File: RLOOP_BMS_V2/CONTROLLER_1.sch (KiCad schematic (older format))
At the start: 29 parts, among them U3 bq76PL536A_HTQFP

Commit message: More WIP
Added connector for 1-Wire sensors if we want to put some sensors on the
heat-sinks. Just need to double check everything with the 3d-models.
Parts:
- U3: symbol bq76PL536A_HTQFP -> bq76PL536A_HTQFP-RESCUE-rLoop_BMS_v2
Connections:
- net labels added: ALERT_H, CONV_H, DRDY_H, FAULT_H
- wire segments 133 -> 138
- no-connect marks 5 -> 1
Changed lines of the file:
@@
 EESchema Schematic File Version 2
+LIBS:rLoop BMS v2-rescue
 LIBS:power
 LIBS:device
@@
 Text GLabel 4700 5750 3    60   Input ~ 0
 GND_1
-NoConn ~ 5200 5100
-NoConn ~ 5300 5100
-NoConn ~ 5400 5100
-NoConn ~ 5500 5100
-$Comp
-L bq76PL536A_HTQFP U3
+$Comp
+L bq76PL536A_HTQFP-RESCUE-rLoop_BMS_v2 U3
 U 1 1 592C9A06
 P 5550 3650
+AR Path="/592C9A06" Ref="U3"  Part="1"
+AR Path="/590D88AD/592C9A06" Ref="U3"  Part="1"
 F 0 "U3" H 5550 3650 60  0000 C CNN
 F 1 "bq76PL536A_HTQFP" H 5550 3900 60  0000 C CNN
@@
 	4300 3750 4400 3750
 Wire Wire Line
-	4300 3550 4300 3750
+	4300 3450 4300 3750
 Wire Wire Line
 	4250 3550 4400 3550
@@
 Wire Wire Line
 	8800 1500 8800 1450
+Text HLabel 5200 5750 3    60   Output ~ 0
+FAULT_H
+Text HLabel 5300 5750 3    60   Output ~ 0
+ALERT_H
+Text HLabel 5400 5750 3    60   Output ~ 0
+DRDY_H
+Text HLabel 5500 5750 3    60   Input ~ 0
+CONV_H
+Wire Wire Line
+	5500 5750 5500 5100
+Wire Wire Line
+	5400 5100 5400 5750
+Wire Wire Line
+	5300 5750 5300 5100
+Wire Wire Line
+	5200 5100 5200 5750
+Wire Wire Line
+	4400 3450 4300 3450
 $EndSCHEMATC

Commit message: more WIP
So close. Need to finish arranging the sild screen and make sure diodes
get put on in the correct orientation.
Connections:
- net GND_1: now also U3.THRM
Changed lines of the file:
@@
 Connection ~ 7500 3800
 Wire Wire Line
-	7100 4250 7100 4900
+	7100 4150 7100 4900
 Wire Wire Line
 	6650 4250 7100 4250
@@
 Wire Wire Line
 	4400 3450 4300 3450
+Wire Wire Line
+	6650 4150 7100 4150
+Connection ~ 7100 4250
 $EndSCHEMATC

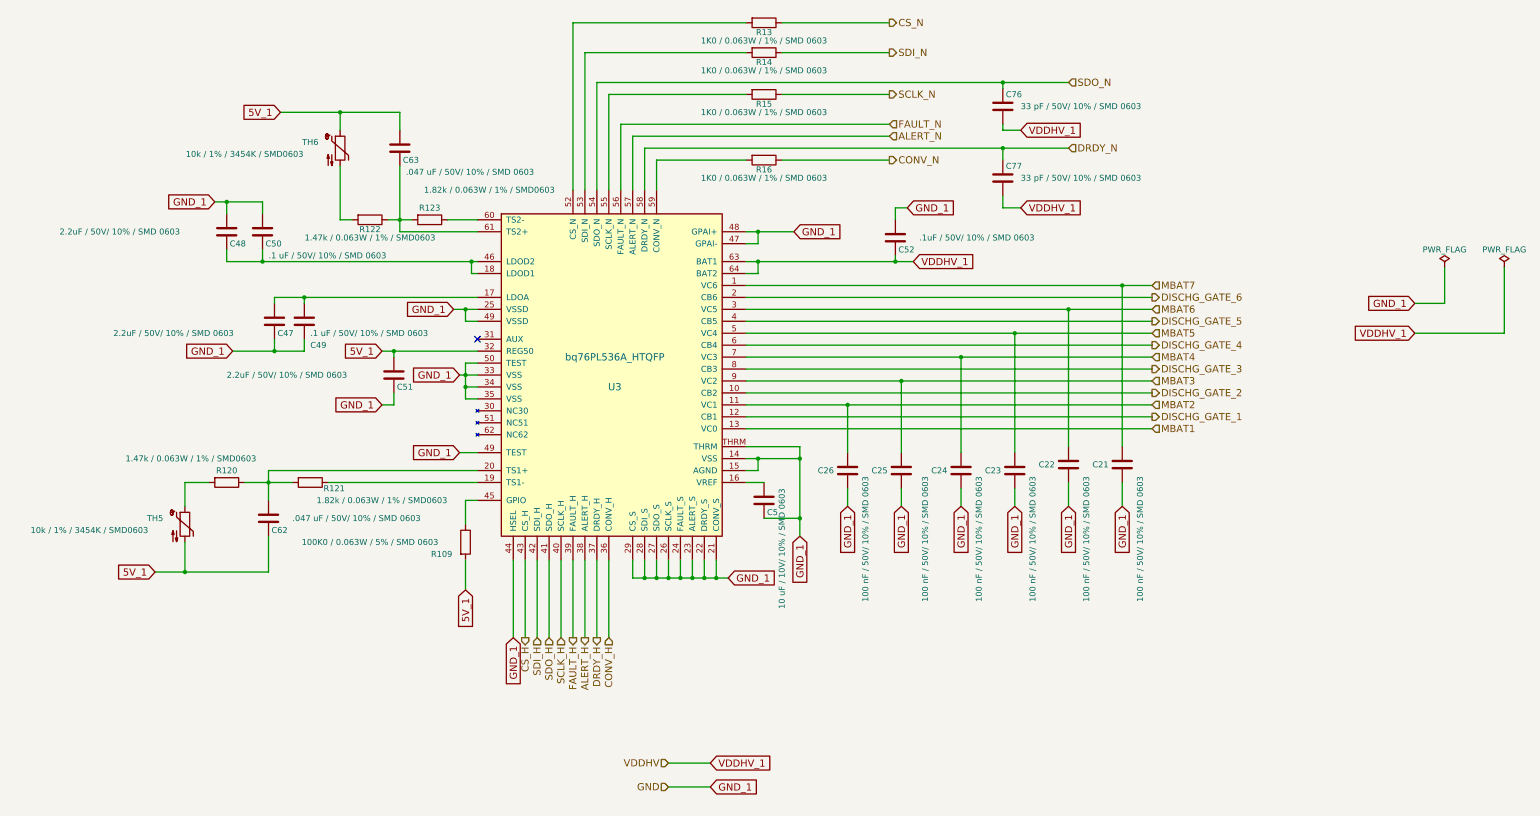
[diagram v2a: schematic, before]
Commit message: Updated page sizes for schematics
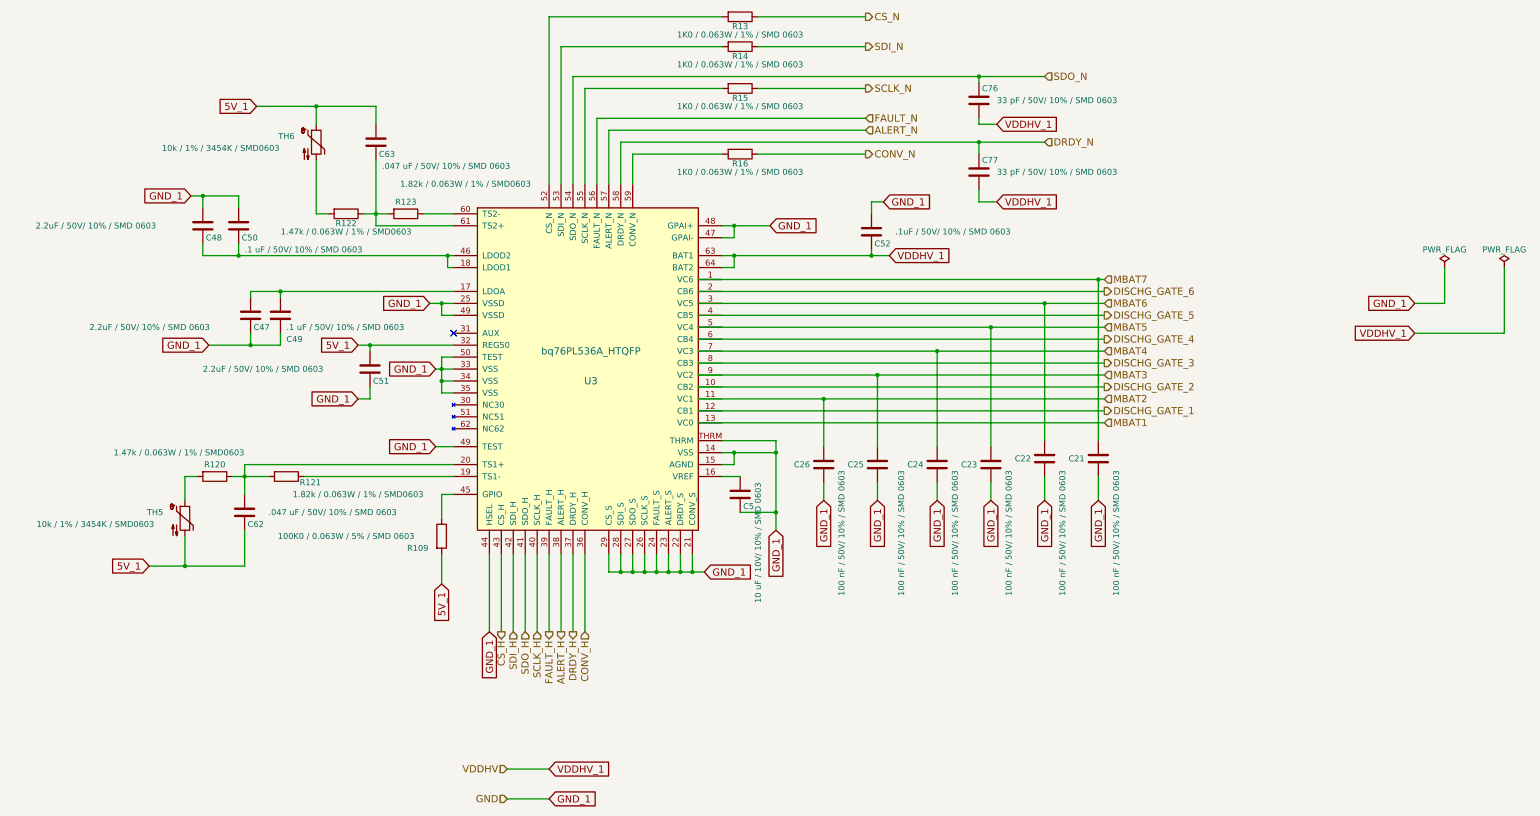
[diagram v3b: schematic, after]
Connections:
- wire segments 139 -> 176
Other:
- moved on the sheet: C21, C22, C23, C24, C25, C26, C47, C48, C49, C5, C50, C51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

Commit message: swapped a few connectors to standardize with the power node and what's readily available
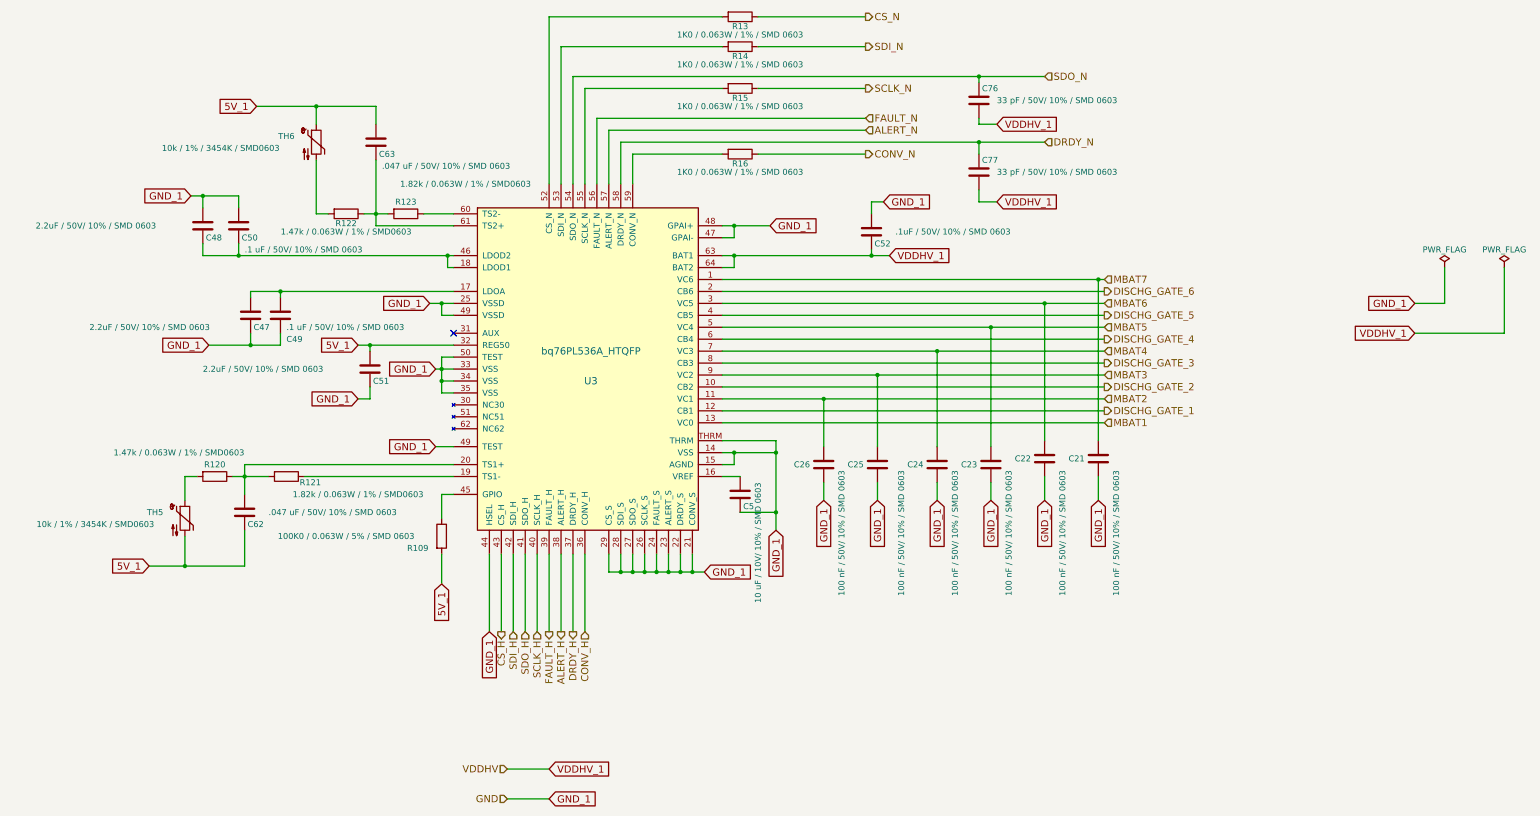
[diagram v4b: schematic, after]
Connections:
- wire segments 176 -> 139
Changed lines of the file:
@@
 	4650 7100 5000 7100
 Wire Wire Line
-	6250 2750 9600 2750
-Wire Wire Line
-	9600 2750 9650 2750
-Wire Wire Line
-	9650 2850 6250 2850
-Wire Wire Line
-	6250 3050 9650 3050
-Wire Wire Line
-	6250 2950 9150 2950
-Wire Wire Line
-	9150 2950 9650 2950
-Wire Wire Line
-	6250 3150 8700 3150
-Wire Wire Line
-	8700 3150 9650 3150
-Wire Wire Line
-	9650 3250 6250 3250
-Wire Wire Line
-	6250 3350 8250 3350
-Wire Wire Line
-	8250 3350 9650 3350
-Wire Wire Line
-	9650 3450 6250 3450
-Wire Wire Line
-	6450 2550 6550 2550
-Wire Wire Line
-	6550 2550 7700 2550
-Wire Wire Line
-	7700 2550 7850 2550
+	6450 2750 9650 2750
+Wire Wire Line
+	6450 2950 9650 2950
+Wire Wire Line
+	6450 3150 9650 3150
+Wire Wire Line
+	6450 3350 9650 3350
+Wire Wire Line
+	6450 2550 7850 2550
 Wire Wire Line
 	6450 2650 6550 2650
@@
 Connection ~ 6550 2550
 Wire Wire Line
-	6250 3550 7750 3550
-Wire Wire Line
-	7750 3550 9650 3550
-Wire Wire Line
-	9650 3650 6250 3650
-Wire Wire Line
-	6250 3750 7300 3750
-Wire Wire Line
-	7300 3750 9650 3750
-Wire Wire Line
-	9650 3850 6250 3850
-Wire Wire Line
-	6250 3950 9650 3950
+	6450 3550 9650 3550
+Wire Wire Line
+	6450 3750 9650 3750
 Wire Wire Line
 	9600 4600 9600 4400
@@
 Connection ~ 7300 3750
 Wire Wire Line
-	6900 4100 6900 4200
-Wire Wire Line
-	6900 4200 6900 4700
-Wire Wire Line
-	6900 4700 6900 4850
-Wire Wire Line
-	6450 4200 6550 4200
-Wire Wire Line
-	6550 4200 6900 4200
+	6900 4100 6900 4850
+Wire Wire Line
+	6450 4200 6900 4200
 Wire Wire Line
 	6450 4300 6550 4300
@@
 	4100 3700 4200 3700
 Wire Wire Line
-	4100 3400 4100 3500
-Wire Wire Line
-	4100 3500 4100 3600
-Wire Wire Line
-	4100 3600 4100 3700
-Wire Wire Line
-	4050 3500 4100 3500
-Wire Wire Line
-	4100 3500 4200 3500
+	4100 3400 4100 3700
+Wire Wire Line
+	4050 3500 4200 3500
 Connection ~ 4100 3500
 Wire Wire Line
@@
 Connection ~ 4100 3600
 Wire Wire Line
-	4000 2950 4100 2950
-Wire Wire Line
-	4100 2950 4200 2950
+	4000 2950 4200 2950
 Wire Wire Line
 	4200 3050 4100 3050
@@
 Connection ~ 4100 2950
 Wire Wire Line
-	3400 3300 3500 3300
-Wire Wire Line
-	3500 3300 4200 3300
+	3400 3300 4200 3300
 Wire Wire Line
 	4050 4150 4200 4150
 Wire Wire Line
-	5500 5200 5600 5200
-Wire Wire Line
-	5600 5200 5700 5200
-Wire Wire Line
-	5700 5200 5800 5200
-Wire Wire Line
-	5800 5200 5900 5200
-Wire Wire Line
-	5900 5200 6000 5200
-Wire Wire Line
-	6000 5200 6100 5200
-Wire Wire Line
-	6100 5200 6200 5200
-Wire Wire Line
-	6200 5200 6300 5200
+	5500 5200 6300 5200
 Wire Wire Line
 	6200 5200 6200 5050
@@
 Connection ~ 5600 5200
 Wire Wire Line
-	6450 2300 6550 2300
-Wire Wire Line
-	6550 2300 6850 2300
+	6450 2300 6850 2300
 Wire Wire Line
 	6450 2400 6550 2400
@@
 	5600 1950 5600 1600
 Wire Wire Line
-	5600 1600 8600 1600
-Wire Wire Line
-	8600 1600 9150 1600
+	5600 1600 9150 1600
 Wire Wire Line
 	5700 1950 5700 1700
@@
 	3500 3750 3500 3650
 Wire Wire Line
-	2000 2050 2100 2050
-Wire Wire Line
-	2100 2050 2400 2050
+	2000 2050 2400 2050
 Wire Wire Line
 	2100 2050 2100 2150
@@
 	2100 2450 2100 2550
 Wire Wire Line
-	2100 2550 2400 2550
-Wire Wire Line
-	2400 2550 4150 2550
-Wire Wire Line
-	4150 2550 4200 2550
+	2100 2550 4200 2550
 Wire Wire Line
 	2400 2450 2400 2550
@@
 	2500 2900 2500 2850
 Wire Wire Line
-	2500 2850 2750 2850
-Wire Wire Line
-	2750 2850 4200 2850
+	2500 2850 4200 2850
 Wire Wire Line
 	2750 2850 2750 2900
@@
 Connection ~ 4150 2550
 Wire Wire Line
-	2150 3300 2500 3300
-Wire Wire Line
-	2500 3300 2750 3300
+	2150 3300 2750 3300
 Wire Wire Line
 	2500 3300 2500 3200
@@
 	3550 2300 4200 2300
 Wire Wire Line
-	3550 1750 3550 2200
-Wire Wire Line
-	3550 2200 3550 2300
-Wire Wire Line
-	3450 2200 3550 2200
-Wire Wire Line
-	3550 2200 3650 2200
+	3550 1750 3550 2300
+Wire Wire Line
+	3450 2200 3650 2200
 Connection ~ 3550 2200
 Wire Wire Line
@@
 	3050 2200 3050 1750
 Wire Wire Line
-	2550 1300 3050 1300
-Wire Wire Line
-	3050 1300 3550 1300
+	2550 1300 3550 1300
 Wire Wire Line
 	3050 1300 3050 1450
@@
 	1950 4400 2050 4400
 Wire Wire Line
-	1650 5150 1950 5150
-Wire Wire Line
-	1950 5150 2450 5150
+	1650 5150 2450 5150
 Wire Wire Line
 	1950 5150 1950 4900
@@
 Connection ~ 1950 5150
 Wire Wire Line
-	2350 4400 2450 4400
-Wire Wire Line
-	2450 4400 2650 4400
-Wire Wire Line
-	2450 4300 2450 4400
-Wire Wire Line
-	2450 4400 2450 4550
+	2350 4400 2650 4400
+Wire Wire Line
+	2450 4300 2450 4550
 Connection ~ 2450 4400
 Wire Wire Line
@@
 Connection ~ 8600 1600
 Wire Wire Line
-	5200 1050 8600 1050
-Wire Wire Line
-	8600 1050 9150 1050
+	5200 1050 9150 1050
 Wire Wire Line
 	8600 1100 8600 1050
@@
 	6450 4100 6900 4100
 Connection ~ 6900 4200
+Wire Wire Line
+	9650 3950 6450 3950
+Wire Wire Line
+	6450 3850 9650 3850
+Wire Wire Line
+	9650 3650 6450 3650
+Wire Wire Line
+	9650 3450 6450 3450
+Wire Wire Line
+	9650 3250 6450 3250
+Wire Wire Line
+	9650 3050 6450 3050
+Wire Wire Line
+	9650 2850 6450 2850
 $EndSCHEMATC
